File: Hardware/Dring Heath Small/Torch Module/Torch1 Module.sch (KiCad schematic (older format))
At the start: 75 parts, among them J1 Torch, J10 Module conn, J11 Conn_01x18_Male, J12 Conn_01x02_Male, J14 Conn_01x02_Male, J15 Module conn, J2 Module3, J3 Conn_01x18_Male, J4 Limit, J6 Motor, J7 Module1, J8 Torch, J9 2.54 pin, K1 G6E, Q1 IRLML2402, Q2 IRLML2402, Q3 IRLML2402, Q4 IRLML2402, Q5 IRLML2402, U1 ULN2002, U2 NCV8114ASN150T1G, U3 ADS1115IDGS

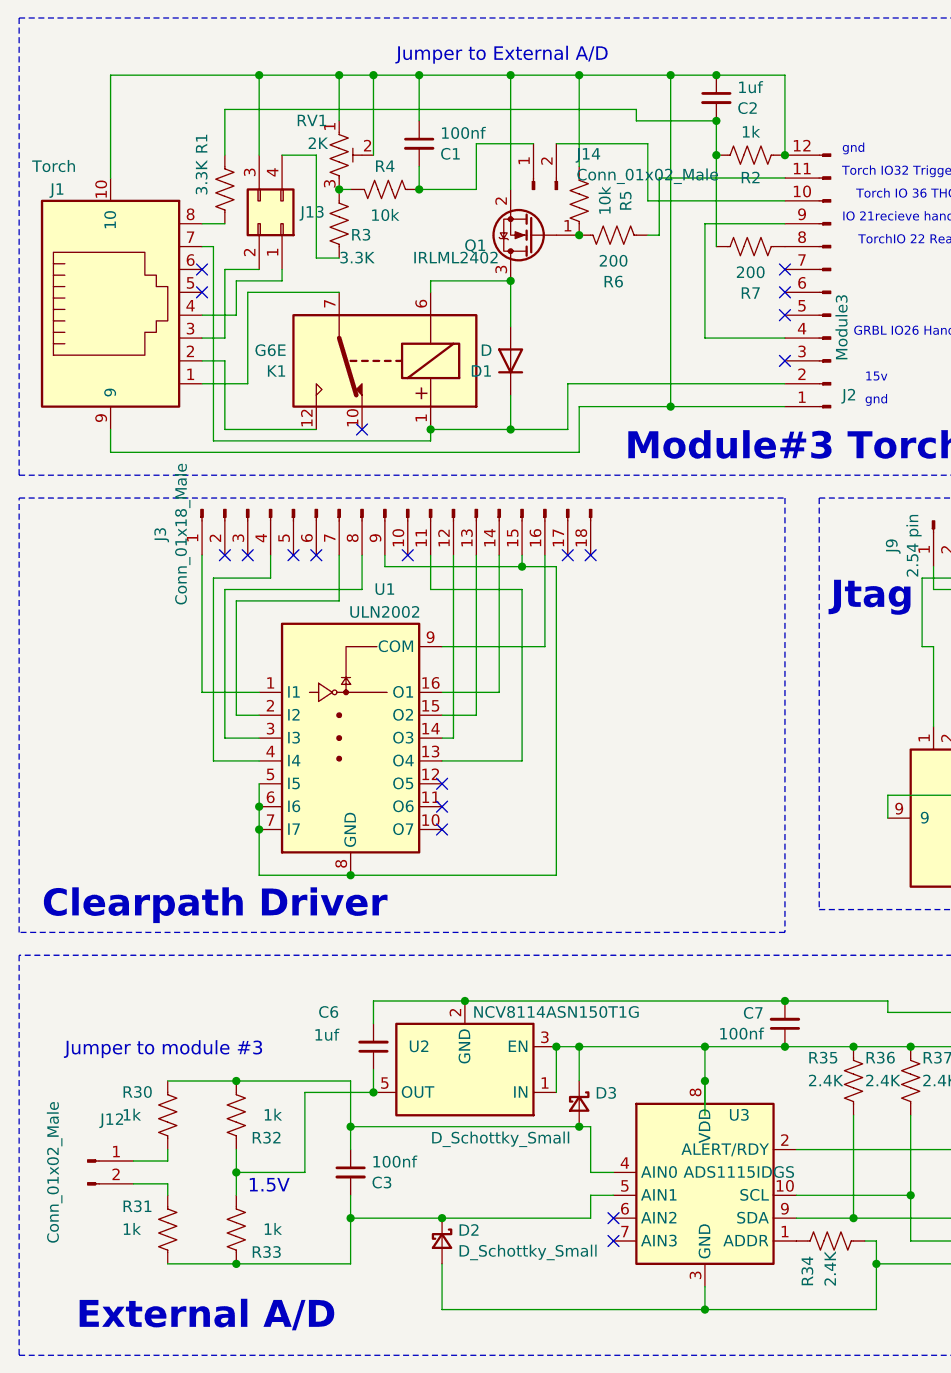
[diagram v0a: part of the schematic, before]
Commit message: Torch1Module.sch alternate A/D input
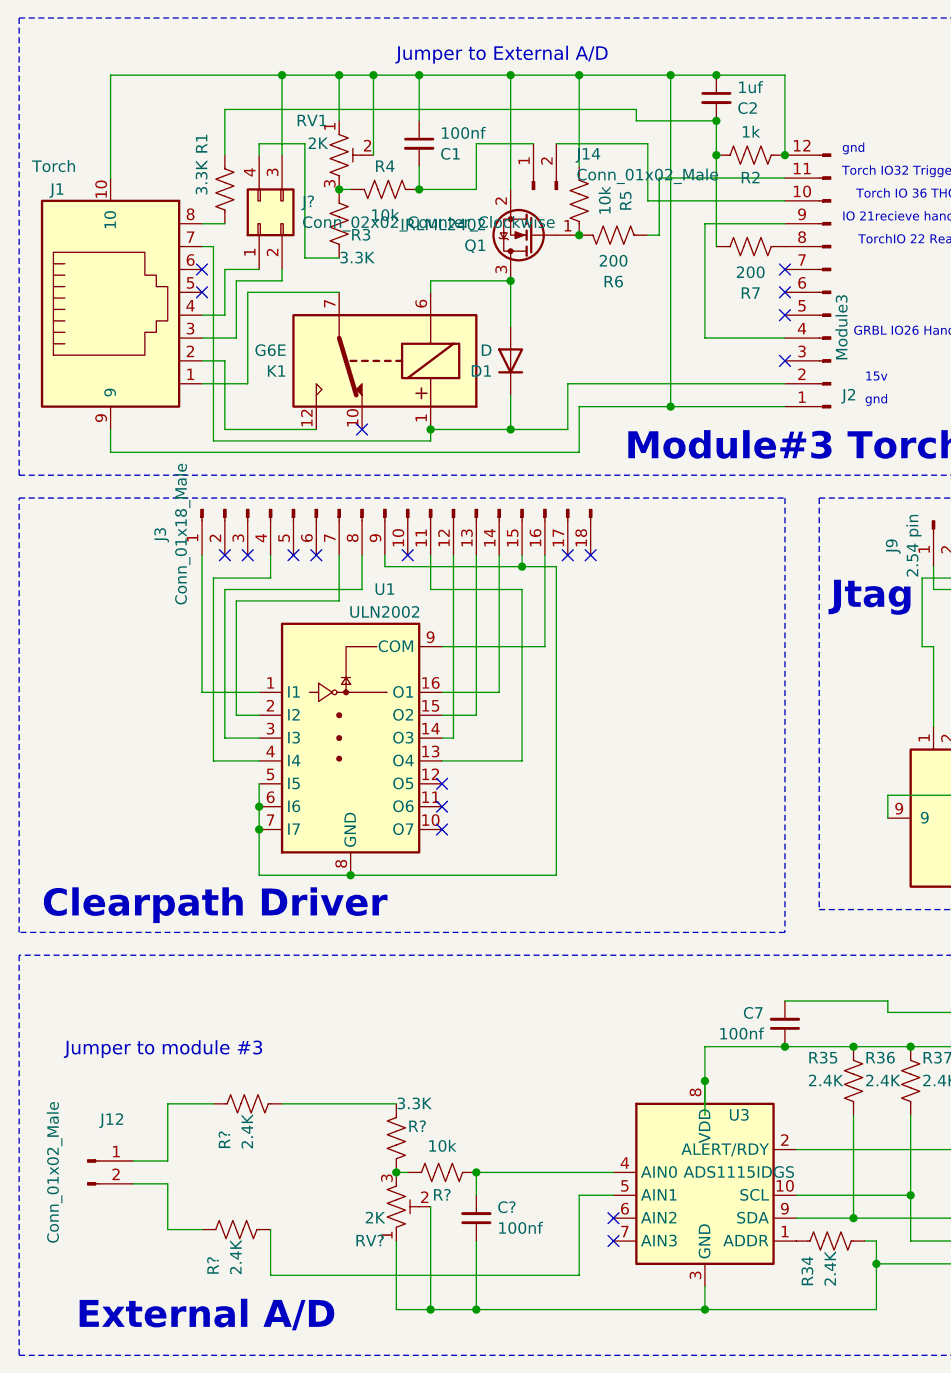
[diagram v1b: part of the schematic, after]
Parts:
- removed C3: 100nf, Capacitor_SMD:C_0603_1608Metric_Pad1.08x0.95mm_HandSolder, symbol Device:C_Small
- removed C6: 1uf, Capacitor_SMD:C_0603_1608Metric_Pad1.08x0.95mm_HandSolder, symbol Device:C_Small
- removed D2, D3: D_Schottky_Small, Diode_SMD:D_0805_2012Metric_Pad1.15x1.40mm_HandSolder, symbol Device:D_Schottky_Small
- removed J13: ~, Connector_PinHeader_2.54mm:PinHeader_2x02_P2.54mm_Vertical, symbol Connector_Generic:Conn_02x02_Counter_Clockwise
- removed R30, R31, R32, R33: 1k, Resistor_SMD:R_0603_1608Metric_Pad0.98x0.95mm_HandSolder, symbol Device:R_US
- removed U2: NCV8114ASN150T1G, Package_TO_SOT_SMD:TSOT-23-5, symbol Regulator_Linear:NCV8114ASN150T1G
- added C?: 100nf, Capacitor_SMD:C_0603_1608Metric_Pad1.08x0.95mm_HandSolder, symbol Device:C_Small
- added J?: Conn_02x02_Counter_Clockwise, symbol Connector_Generic:Conn_02x02_Counter_Clockwise
- added R?: 10k, Resistor_SMD:R_0603_1608Metric_Pad0.98x0.95mm_HandSolder, symbol Device:R_US
- added R?: 3.3K, Resistor_SMD:R_0603_1608Metric_Pad0.98x0.95mm_HandSolder, symbol Device:R_US
- added R? (x2): 2.4K, Resistor_SMD:R_0603_1608Metric_Pad0.98x0.95mm_HandSolder, symbol Device:R_US
- added RV?: 2K, Potentiometer_THT:Potentiometer_Bourns_3339S_Horizontal, symbol Device:R_POT_TRIM_US
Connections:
- net at C1.1, C2.1, J1.10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: now also J?.3 (Pin_3)
- net at J1.3: now also J?.2 (Pin_2)
- net at J1.4: now also J?.1 (Pin_1)
- net at R3.1: now also J?.4 (Pin_4)
- net at C7.2, FB1.2, R34.2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: now also C?.1, RV?.1, RV?.2
- net at U3.4 (AIN0): now also C?.2, R?.1
- net at U3.5 (AIN1): now also R?.2
- net at J12.1 (Pin_1): now also R?.1
- net at J12.2 (Pin_2): now also R?.1
- new net: R?.2, R?.2, RV?.3
- new net: R?.1, R?.2
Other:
- note removed: "1.5V"
